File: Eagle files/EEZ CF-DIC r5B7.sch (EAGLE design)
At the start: 277 parts, among them IC1 VIPer35L, IC2 SI8233BB-D-IS1, IC3 LM5041B, IC4 LM258D, IC5 IR11688STRPBF, IC6 LM258D, IC7 TL103W, P1 T910W-50K, Q1 MMBT5551, Q10 BC856C, Q2 C3M0280090D, Q3 C3M0280090D, Q4 NYC0102BLT1G, Q5 IPW60R120P7, Q6 IPW60R120P7, Q7 FDD86250-F085, Q8 FDD86250-F085, Q9 BC856C, X1 39-30-3035, X2 22-05-7095, X3 B2B-ZR, X4 39-30-1020

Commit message: r5B7 BOM
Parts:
- C27, C75: value 47p -> 47p/200V
- C41: value 4n7/500V -> 2n2/1kV
- C57: value UPW1J152MHD -> UVZ1J222MHD
- C63, C70: value 4n7/500V -> 2n2/1kV; device rcl:C-EUC1206 -> rcl:C-EUC1210
- D11, D14: value 1N5819HW-7-F -> N.C.
- Q5, Q6: value IPW60R120P7 -> IRFP4332PBF
- R32: device rcl:R-EU_R1206 -> rcl:R-EU_R0805
- R70, R76: value 1K -> 1K8
- R74: value 100K -> 86K6
- ZD1: value BZX384-C13 -> BZT52C13; device EEZ_Lib1:ZENER-DIODESOD323 -> EEZ_Lib1:ZENER-DIODESOD123
- ZD3: device EEZ_Lib1:ZENER-DIODESOD323 -> EEZ_Lib1:ZENER-DIODESOD123
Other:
- moved on the sheet: R20
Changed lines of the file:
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@@
 <setting verticaltext="up"/>
 </settings>
-<grid distance="0.1" unitdist="inch" unit="inch" style="lines" multiple="1" display="no" altdistance="0.01" altunitdist="inch" altunit="inch"/>
+<grid distance="0.025" unitdist="inch" unit="inch" style="lines" multiple="4" display="no" altdistance="0.01" altunitdist="inch" altunit="inch"/>
 <layers>
 <layer number="1" name="Top" color="4" fill="1" visible="no" active="no"/>
@@
 <part name="R68" library="rcl" deviceset="R-EU_" device="R2512" value="22R/2-3W"/>
 <part name="R77" library="rcl" deviceset="R-EU_" device="R2512" value="22R/2-3W"/>
-<part name="C63" library="rcl" deviceset="C-EU" device="C1206" value="4n7/500V"/>
-<part name="C70" library="rcl" deviceset="C-EU" device="C1206" value="4n7/500V"/>
+<part name="C63" library="rcl" deviceset="C-EU" device="C1210" value="2n2/1kV"/>
+<part name="C70" library="rcl" deviceset="C-EU" device="C1210" value="2n2/1kV"/>
 <part name="R73" library="rcl" deviceset="R-EU_" device="R0805" value="10R"/>
 <part name="C58" library="rcl" deviceset="C-EU" device="C1206" value="1u/100V"/>
 <part name="C66" library="rcl" deviceset="C-EU" device="C1206" value="4u7"/>
-<part name="C57" library="EEZ_Lib1" deviceset="ECAP" device="H35.5A" value="UPW1J152MHD"/>
+<part name="C57" library="EEZ_Lib1" deviceset="ECAP" device="H35.5A" value="UVZ1J222MHD"/>
 <part name="TP1" library="EEZ_Lib1" deviceset="PCB_TEST_TAB" device="SHIELD"/>
 <part name="R18" library="rcl" deviceset="R-EU_" device="R0805" value="1K"/>
@@
 <part name="C10" library="rcl" deviceset="C-EU" device="C0805" value="1u"/>
 <part name="R79" library="rcl" deviceset="R-EU_" device="R0805" value="470R"/>
-<part name="ZD1" library="EEZ_Lib1" deviceset="ZENER-DIODE" device="SOD323" value="BZX384-C13"/>
+<part name="ZD1" library="EEZ_Lib1" deviceset="ZENER-DIODE" device="SOD123" value="BZT52C13"/>
 <part name="R4" library="rcl" deviceset="R-EU_" device="R0805" value="1K8"/>
 <part name="C4" library="rcl" deviceset="C-EU" device="C0603" value="N.C."/>
@@
 <part name="R1" library="rcl" deviceset="R-EU_" device="R0805" value="120R"/>
 <part name="C1" library="rcl" deviceset="C-EU" device="C0805" value="3n3"/>
-<part name="C27" library="rcl" deviceset="C-EU" device="C0805" value="47p"/>
+<part name="C27" library="rcl" deviceset="C-EU" device="C0805" value="47p/200V"/>
 <part name="C21" library="rcl" deviceset="C-EU" device="C0603" value="100n"/>
 <part name="R17" library="rcl" deviceset="R-EU_" device="R0805" value="16K"/>
@@
 <part name="R12" library="rcl" deviceset="R-EU_" device="R0805" value="120R"/>
 <part name="R15" library="rcl" deviceset="R-EU_" device="R0805" value="120R"/>
-<part name="ZD3" library="EEZ_Lib1" deviceset="ZENER-DIODE" device="SOD323" value="MMSZ5V1T1G"/>
+<part name="ZD3" library="EEZ_Lib1" deviceset="ZENER-DIODE" device="SOD123" value="MMSZ5V1T1G"/>
 <part name="SUPPLY77" library="supply2" deviceset="+12V" device=""/>
 <part name="SUPPLY80" library="supply2" deviceset="GND" device=""/>
@@
 <part name="R87" library="rcl" deviceset="R-EU_" device="R0805" value="86K6"/>
 <part name="C78" library="rcl" deviceset="C-EU" device="C0805" value="470p"/>
-<part name="C75" library="rcl" deviceset="C-EU" device="C0805" value="47p"/>
+<part name="C75" library="rcl" deviceset="C-EU" device="C0805" value="47p/200V"/>
 <part name="R92" library="rcl" deviceset="R-EU_" device="R0805" value="7K5"/>
 <part name="R81" library="rcl" deviceset="R-EU_" device="R0805" value="150K"/>
@@
 <part name="JP5" library="EEZ_Lib1" deviceset="JP3-CUT" device=""/>
 <part name="PE4" library="supply1" deviceset="PE" device=""/>
-<part name="R74" library="rcl" deviceset="R-EU_" device="R0805" value="100K"/>
+<part name="R74" library="rcl" deviceset="R-EU_" device="R0805" value="86K6"/>
 <part name="IC5" library="EEZ_Lib1" deviceset="IR11688" device="" value="IR11688STRPBF"/>
 <part name="C5" library="EEZ_Lib1" deviceset="ECAP" device="PANASONIC_H" value="EEEFK1V470P"/>
@@
 <part name="D10" library="EEZ_Lib1" deviceset="SCHOTTKY" device="-SIC_L" value="C3D02065E"/>
 <part name="C31" library="rcl" deviceset="C-EU" device="C0603" value="10n"/>
-<part name="Q6" library="EEZ_Lib1" deviceset="IRFP240" device="" value="IPW60R120P7"/>
-<part name="Q5" library="EEZ_Lib1" deviceset="IRFP240" device="" value="IPW60R120P7"/>
+<part name="Q6" library="EEZ_Lib1" deviceset="IRFP240" device="" value="IRFP4332PBF"/>
+<part name="Q5" library="EEZ_Lib1" deviceset="IRFP240" device="" value="IRFP4332PBF"/>
 <part name="C48" library="rcl" deviceset="C-EU" device="C0603" value="100n"/>
 <part name="R51" library="rcl" deviceset="R-EU_" device="R0805" value="15K"/>
 <part name="C46" library="rcl" deviceset="C-EU" device="C0805" value="1u"/>
-<part name="R32" library="rcl" deviceset="R-EU_" device="R1206" value="86K6"/>
+<part name="R32" library="rcl" deviceset="R-EU_" device="R0805" value="86K6"/>
 <part name="R47" library="rcl" deviceset="R-EU_" device="R0805" value="8K2"/>
 <part name="R45" library="rcl" deviceset="R-EU_" device="R0805" value="1K"/>
@@
 <part name="Q3" library="EEZ_Lib1" deviceset="IRFP240" device="" value="C3M0280090D"/>
 <part name="R26" library="rcl" deviceset="R-EU_" device="R0805" value="10R"/>
-<part name="D11" library="diode" deviceset="DIODE-" device="SOD323-W" value="1N5819HW-7-F"/>
+<part name="D11" library="diode" deviceset="DIODE-" device="SOD323-W" value="N.C."/>
 <part name="R36" library="rcl" deviceset="R-EU_" device="R0805" value="10R"/>
-<part name="D14" library="diode" deviceset="DIODE-" device="SOD323-W" value="1N5819HW-7-F"/>
+<part name="D14" library="diode" deviceset="DIODE-" device="SOD323-W" value="N.C."/>
 <part name="C45" library="rcl" deviceset="C-EU" device="C0603" value="100n"/>
 <part name="D12" library="EEZ_Lib1" deviceset="SCHOTTKY" device="-TO220" value="C3D03060A"/>
@@
 <part name="OK3" library="EEZ_Lib1" deviceset="TLP291" device="" value="TLP291-GB.SE-T"/>
 <part name="SUPPLY60" library="supply2" deviceset="0V" device=""/>
-<part name="C41" library="rcl" deviceset="C-EU" device="C1210" value="4n7/500V"/>
+<part name="C41" library="rcl" deviceset="C-EU" device="C1210" value="2n2/1kV"/>
 <part name="C35" library="EEZ_Lib1" deviceset="ECAP" device="7.5G_18MM" value="UPH2G151MHD6"/>
 <part name="R44" library="rcl" deviceset="R-EU_" device="R0805" value="10R"/>
@@
 <part name="R7" library="rcl" deviceset="R-EU_" device="R0805" value="4K7"/>
 <part name="JP4" library="jump-0r-smd" deviceset="0R-JUMP" device="A"/>
-<part name="R76" library="rcl" deviceset="R-EU_" device="R0805" value="1K"/>
-<part name="R70" library="rcl" deviceset="R-EU_" device="R0805" value="1K"/>
+<part name="R76" library="rcl" deviceset="R-EU_" device="R0805" value="1K8"/>
+<part name="R70" library="rcl" deviceset="R-EU_" device="R0805" value="1K8"/>
 <part name="C71" library="rcl" deviceset="C-EU" device="C0805" value="47p/200V"/>
 <part name="C59" library="rcl" deviceset="C-EU" device="C0805" value="47p/200V"/>
@@
 <attribute name="VALUE" x="203.2" y="68.58" size="1.778" layer="96" rot="R90"/>
 </instance>
-<instance part="R20" gate="G$1" x="66.04" y="27.94" smashed="yes" rot="MR270">
-<attribute name="NAME" x="64.77" y="28.1686" size="1.778" layer="95" rot="MR0"/>
-<attribute name="VALUE" x="64.77" y="25.908" size="1.778" layer="96" rot="MR0"/>
+<instance part="R20" gate="G$1" x="66.04" y="33.02" smashed="yes" rot="MR270">
+<attribute name="NAME" x="64.77" y="33.2486" size="1.778" layer="95" rot="MR0"/>
+<attribute name="VALUE" x="64.77" y="30.988" size="1.778" layer="96" rot="MR0"/>
 </instance>
 <instance part="R14" gate="G$1" x="66.04" y="83.82" smashed="yes" rot="R270">
@@
 <wire x1="53.34" y1="17.78" x2="48.26" y2="17.78" width="0.1524" layer="91"/>
 <pinref part="R20" gate="G$1" pin="2"/>
-<wire x1="66.04" y1="22.86" x2="66.04" y2="17.78" width="0.1524" layer="91"/>
+<wire x1="66.04" y1="27.94" x2="66.04" y2="17.78" width="0.1524" layer="91"/>
 <junction x="66.04" y="17.78"/>
 <pinref part="D9" gate="G$1" pin="A"/>
@@
 <pinref part="IC1" gate="G$1" pin="BR"/>
 <pinref part="R20" gate="G$1" pin="1"/>
-<wire x1="66.04" y1="33.02" x2="66.04" y2="55.88" width="0.1524" layer="91"/>
+<wire x1="66.04" y1="38.1" x2="66.04" y2="55.88" width="0.1524" layer="91"/>
 <pinref part="R14" gate="G$1" pin="2"/>
 <wire x1="66.04" y1="55.88" x2="66.04" y2="78.74" width="0.1524" layer="91"/>
@@
 <instance part="D11" gate="G$1" x="154.94" y="157.48" smashed="yes" rot="R180">
 <attribute name="NAME" x="152.654" y="159.2326" size="1.778" layer="95"/>
-<attribute name="VALUE" x="148.082" y="154.5336" size="1.27" layer="96"/>
+<attribute name="VALUE" x="152.527" y="153.8986" size="1.778" layer="96"/>
 </instance>
 <instance part="R36" gate="G$1" x="147.32" y="127" smashed="yes">
@@
 <instance part="D14" gate="G$1" x="152.4" y="121.92" smashed="yes" rot="R180">
 <attribute name="NAME" x="150.114" y="123.6726" size="1.778" layer="95"/>
-<attribute name="VALUE" x="146.177" y="118.9736" size="1.27" layer="96"/>
+<attribute name="VALUE" x="150.622" y="118.3386" size="1.778" layer="96"/>
 </instance>
 <instance part="C45" gate="G$1" x="109.22" y="88.9" smashed="yes" rot="R90">
@@
 </instance>
 <instance part="C57" gate="G$1" x="149.86" y="157.48" smashed="yes">
-<attribute name="NAME" x="151.003" y="157.9626" size="1.778" layer="95"/>
-<attribute name="VALUE" x="152.2476" y="157.607" size="1.27" layer="96" rot="R270"/>
+<attribute name="NAME" x="150.368" y="157.9626" size="1.778" layer="95"/>
+<attribute name="VALUE" x="150.368" y="152.8826" size="1.27" layer="96"/>
 </instance>
 <instance part="SUPPLY12" gate="GND" x="149.86" y="139.7" smashed="yes">

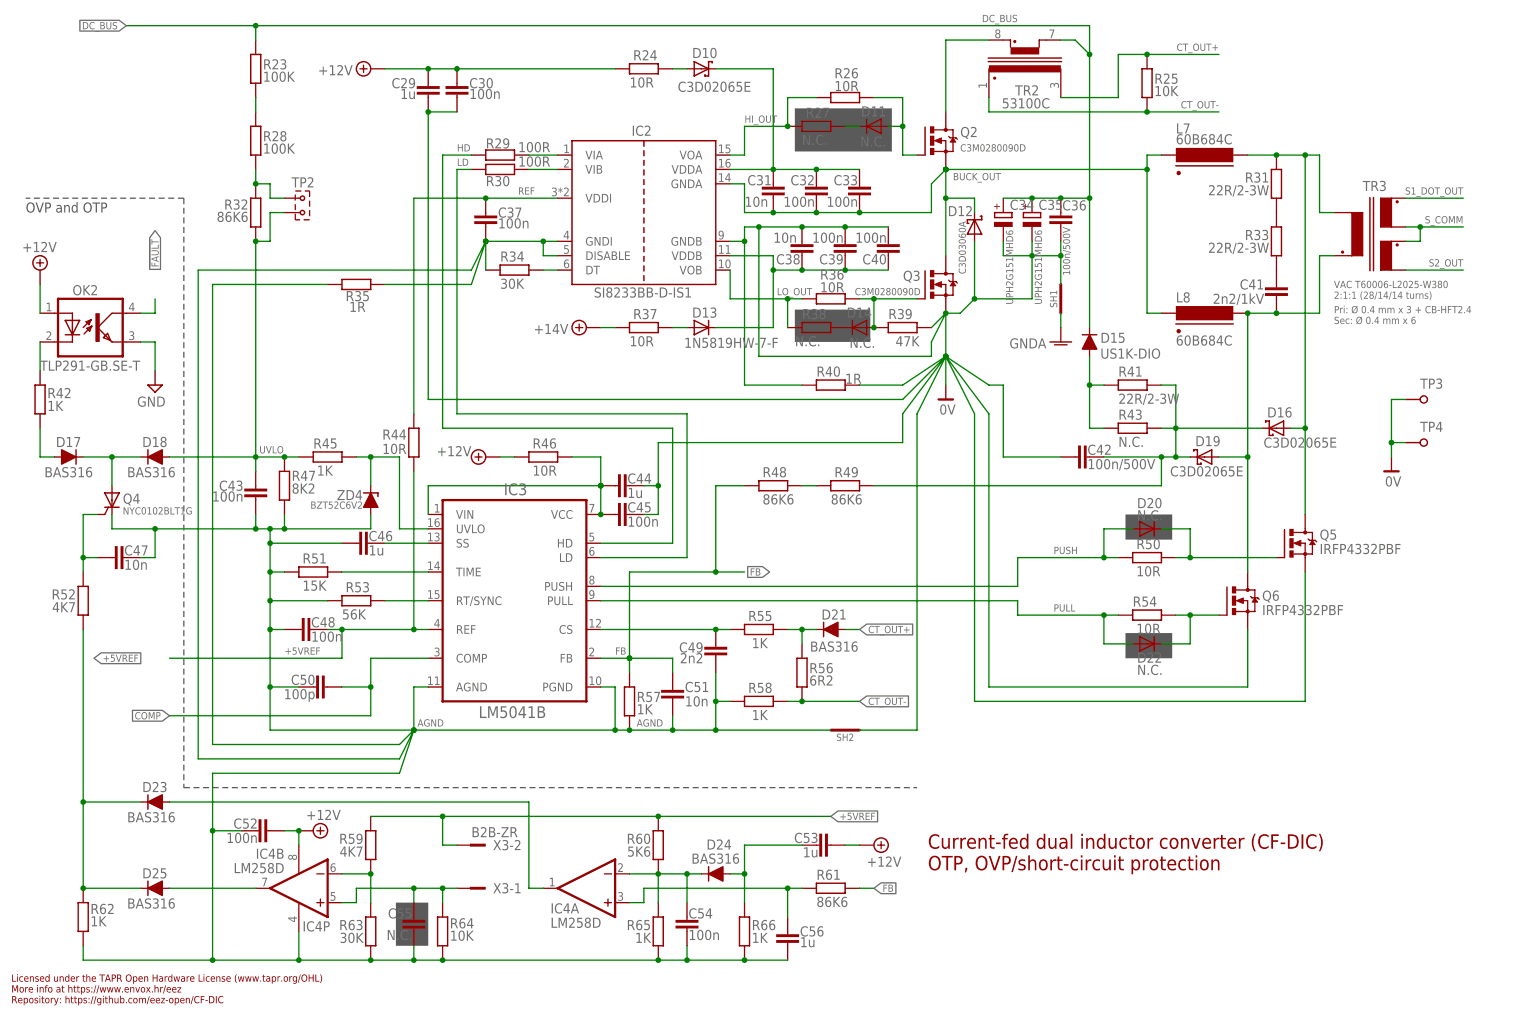
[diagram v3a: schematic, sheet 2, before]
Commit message: NFB compensation and Viper Rovp adjustment
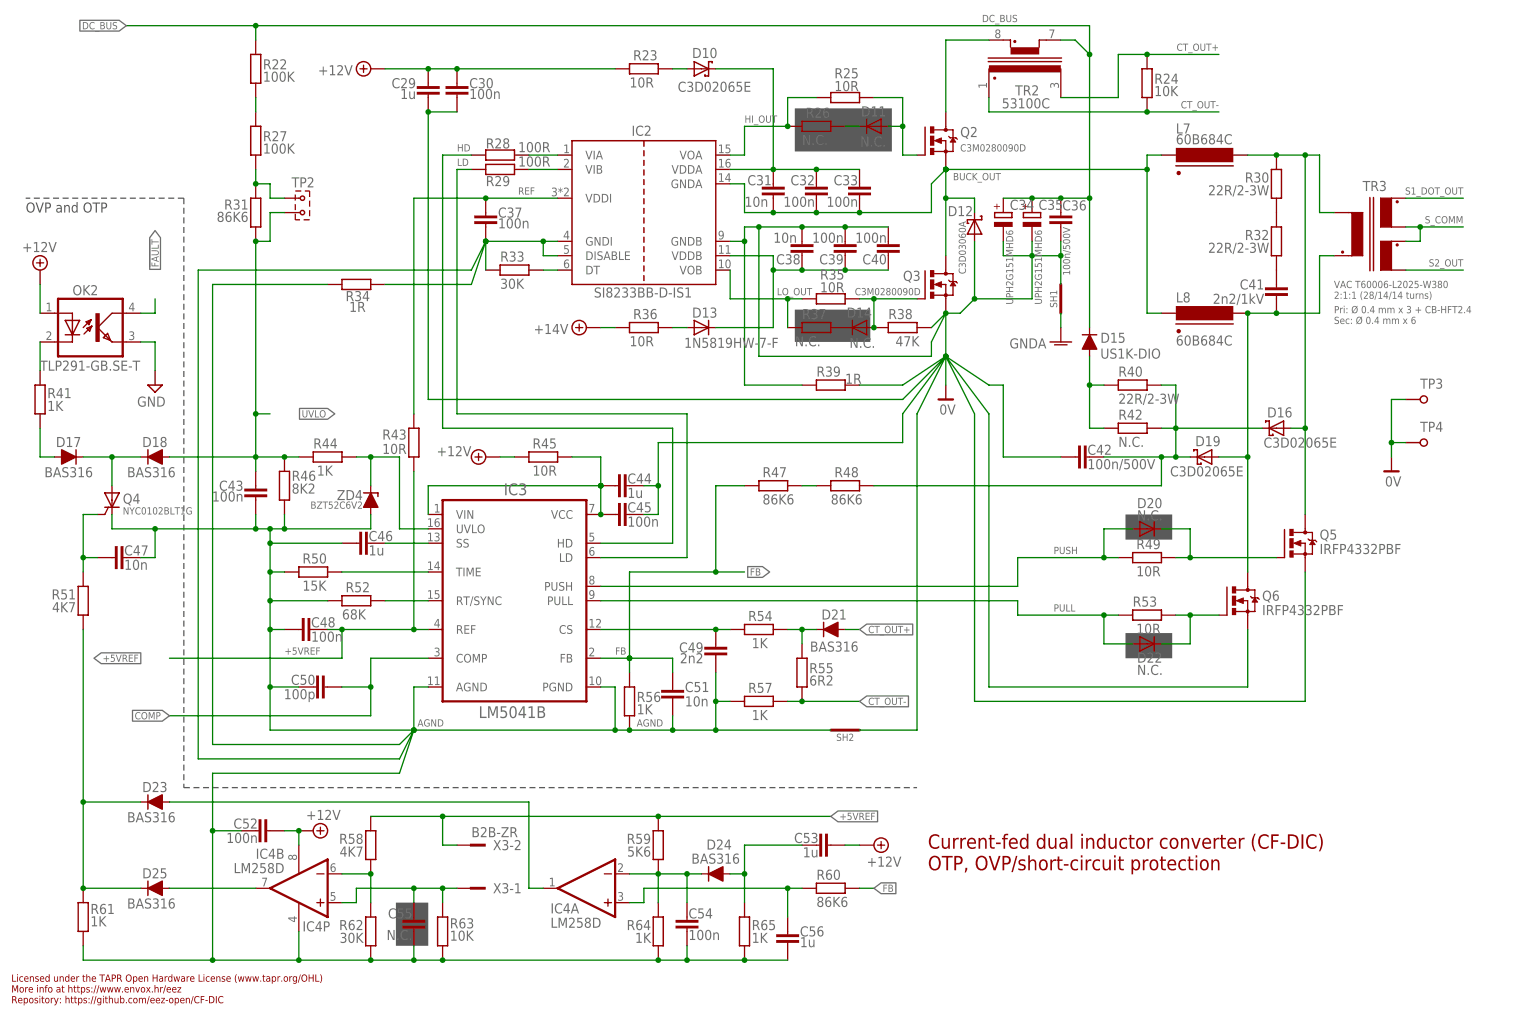
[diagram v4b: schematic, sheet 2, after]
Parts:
- removed R101: 39K, rcl:R-EU_R0805
- C14: value 2n2/1kV -> 1n/1kV
- C73: value 1n -> 2n2
- C78: value 470p -> 1n
- D7: value SS100B -> SS110B
- L9: value IHLP2020CZER3R3M11 -> 3u3/5A; device EEZ_inductors_and_transformers:IHLP-2020BZ-11 -> EEZ_inductors_and_transformers:COILCRAFT_HPI0630
- R100: value 18K -> 39K
- R11, R8: value 36K -> 100K
- R16: value N.C. -> 30K
- R17: value 16K -> 1K
- R18: value 1K -> 1K8
- R20: value 1K8 -> 47K
- R21: value 47K -> 1K
- R22: value 1K -> 100K; device rcl:R-EU_R0805 -> rcl:R-EU_R1206
- R23: value 100K -> 10R; device rcl:R-EU_R1206 -> rcl:R-EU_R0805
- R24: value 10R -> 10K
- R25: value 10K -> 10R
- R26, R37: value 10R -> N.C.
- R27: value N.C. -> 100K; device rcl:R-EU_R0805 -> rcl:R-EU_R1206
- R28: value 100K -> 100R; device rcl:R-EU_R1206 -> rcl:R-EU_R0805
- R30: value 100R -> 22R/2-3W; device rcl:R-EU_R0805 -> rcl:R-EU_R2512
- R31: value 22R/2-3W -> 86K6; device rcl:R-EU_R2512 -> rcl:R-EU_R0805
- R32: value 86K6 -> 22R/2-3W; device rcl:R-EU_R0805 -> rcl:R-EU_R2512
- R33: value 22R/2-3W -> 30K; device rcl:R-EU_R2512 -> rcl:R-EU_R0805
- R34: value 30K -> 1R
- R35: value 1R -> 10R
- R38: value N.C. -> 47K
- R39: value 47K -> 1R
- R40: value 1R -> 22R/2-3W; device rcl:R-EU_R0805 -> rcl:R-EU_R2512
- R41: value 22R/2-3W -> 1K; device rcl:R-EU_R2512 -> rcl:R-EU_R0805
- R42: value 1K -> N.C.; device rcl:R-EU_R0805 -> rcl:R-EU_R2512
- R43, R71: value N.C. -> 10R; device rcl:R-EU_R2512 -> rcl:R-EU_R0805
- R44, R54, R75: value 10R -> 1K
- R45: value 1K -> 10R
- R46: value 10R -> 8K2
- R47: value 8K2 -> 86K6
- R49, R74: value 86K6 -> 10R
- R50: value 10R -> 15K
- R51: value 15K -> 4K7
- R52: value 4K7 -> 68K
- R53: value 56K -> 10R
- R55: value 1K -> 6R2
- R56: value 6R2 -> 1K
- R58, R83: value 1K -> 4K7
- R59: value 4K7 -> 5K6
- R60: value 5K6 -> 86K6
- R61: value 86K6 -> 1K
- R62: value 1K -> 30K
- R63: value 30K -> 10K
- R64, R82: value 10K -> 1K
- R66: value 1K -> 120R
- R67: value 120R -> 22R/2-3W; device rcl:R-EU_R0805 -> rcl:R-EU_R2512
- R68: value 22R/2-3W -> N.C.; device rcl:R-EU_R2512 -> rcl:R-EU_R1210
- R69: value N.C. -> 1K; device rcl:R-EU_R1210 -> rcl:R-EU_R0805
- R70: value 1K8 -> N.C.; device rcl:R-EU_R0805 -> rcl:R-EU_R2512
- R73: value 10R -> 86K6
- R76: value 1K8 -> 22R/2-3W; device rcl:R-EU_R0805 -> rcl:R-EU_R2512
- R77: value 22R/2-3W -> 10K; device rcl:R-EU_R2512 -> rcl:R-EU_R0805
- R78: value 10K -> 470R
- R80: value 470R -> 150K
- R81: value 150K -> 10K
- R84: value 30K -> 1K8
- R85: value 1K8 -> 1K
- R86: value 1K -> 27K
- R87: value 86K6 -> 1K8
- R88: value 1K8 -> 3K3
- R89: value 3K3 -> 1K
- R90: value 1K -> 5K6
- R91: value 5K6 -> 7K5
- R92: value 7K5 -> 220R
- R93: value 220R -> N.C.
- R95: value N.C. -> 10K
- R97: value 10K -> 180K
- R98: value 180K -> 39K
- R99: value 39K -> 18K
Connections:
- net +12V: now also R23.2, R36.2, R45.2; no longer R24.2, R37.2, R46.2
- net +2.5VREF: now also R81.2, R87.1; no longer R82.2, R88.1
- net +5VREF: now also R43.1, R58.2, R95.1, R97.1; no longer R44.1, R60.2, R96.1, R98.1
- net +6V_REC: now also R17.1; no longer R18.1
- net 0V: now also R18.2, R38.2, R39.1; no longer R21.2, R40.1, R40.2
- net AGND: now also R33.1, R34.2, R46.2, R50.2, R52.2, R56.2, R61.2, R96.2, R99.2; no longer R100.2, R35.1, R35.2, R47.2, R51.2, R53.2, R58.2, R66.2, R97.2
- net AUX_AC: no longer R16.2
- net CLAMP_C: now also R40.1, R42.1, R48.2; no longer R41.1, R43.1, R49.2
- net CT_OUT+: now also R24.1; no longer R25.1
- net CT_OUT-: now also R24.2, R55.2, R57.1; no longer R25.2, R56.2, R58.1
- net DC_BUS: now also R22.1; no longer R23.1
- net FB: now also R47.1, R56.1, R60.1; no longer R48.1, R57.1, R61.1
- net FB2: now also R21.1; no longer R22.1
- net G1_OUT: now also R71.1; no longer R72.1
- net G2_OUT: now also R74.1; no longer R75.1
- net GATE1: now also R71.2; no longer R72.2
- net GATE2: now also R74.2; no longer R75.2
- net GND: now also R70.1, R73.2; no longer R71.1, R74.2
- net HD: now also R28.2; no longer R29.2
- net HI_OUT: now also R25.2; no longer R27.2
- net LD: now also R29.2; no longer R30.2
- net LO_OUT: now also R35.1, R37.1; no longer R36.1, R38.1
- net L_PUSH: now also R30.2; no longer R31.2
- net N$10: now also R86.1, R90.1; no longer R87.1, R91.1
- net N$100: now also R51.1; no longer R52.1
- net N$11: now also R79.2; no longer R80.2
- net N$12: now also R80.1, R84.2; no longer R81.1, R85.2
- net N$13: now also R49.1; no longer R50.1
- net N$130: now also R41.2; no longer R42.2
- net N$132: now also R77.2, R81.1; no longer R78.2, R82.1
- net N$134: now also R92.2; no longer R93.2
- net N$135: now also R17.2; no longer R18.2
- net N$14: now also R53.1; no longer R54.1
- net N$141: no longer R17.1
- net N$152: now also R20.1; no longer R21.1
- net N$155: now also R16.2; no longer R17.2
- net N$16: now also R78.2; no longer R79.2
- net N$17: now also R32.1; no longer R33.1
- net N$18: now also R73.1; no longer R74.1
- net N$19: now also R52.1; no longer R53.1
- net N$2: now also R27.2, R31.1; no longer R28.2, R32.1
- net N$20: now also R18.1; no longer R20.1
- net N$21: now also R25.1; no longer R26.1
- net N$22: now also R50.1; no longer R51.1
- net N$25: now also R44.1; no longer R45.1
- net N$26: now also R58.1, R62.1; no longer R59.1, R63.1
- net N$28: now also R83.2; no longer R84.2
- net N$29: now also R35.2, R38.1; no longer R36.2, R39.1
- net N$30: now also R47.2, R48.1; no longer R48.2, R49.1
- net N$31: now also R23.1; no longer R24.1
- net N$32: now also R41.1; no longer R42.1
- net N$34: now also R60.2; no longer R61.2
- net N$35: now also R40.2, R42.2; no longer R41.2, R43.2
- net N$36: now also R28.1; no longer R29.1
- net N$37: now also R54.2; no longer R55.2
- net N$40: now also R29.1; no longer R30.1
- net N$42: now also R63.1; no longer R64.1
- net N$45: now also R26.1; no longer R27.1
- net N$46: now also R72.1, R87.2; no longer R73.1, R89.2
- net N$48: now also R33.2; no longer R34.2
- net N$5: now also R30.1, R32.2; no longer R31.1, R33.2
- net N$50: now also R83.1, R90.2, R93.2; no longer R85.1, R92.2, R94.2
- net N$51: now also R51.2, R61.1; no longer R52.2, R62.1
- net N$52: now also R37.2; no longer R38.2
- net N$53: now also R77.1, R82.2; no longer R78.1, R83.2
- net N$54: now also R45.1; no longer R46.1
- net N$56: now also R54.1; no longer R56.1
- net N$59: now also R65.1; no longer R66.1
- net N$6: now also R22.2, R27.1; no longer R23.2, R28.1
- net N$61: now also R96.1; no longer R97.1
- net N$62: now also R95.2; no longer R96.2
- net N$63: now also R36.1; no longer R37.1
- net N$64: now also R82.1, R85.2, R89.1; no longer R83.1, R86.2, R90.1
- net N$66: now also R76.2; no longer R77.2
- net N$67: now also R67.2; no longer R68.2
- net N$68: now also R98.2, R99.1; no longer R101.1, R99.2
- net N$7: now also R59.1, R64.1; no longer R60.1, R65.1
- net N$70: now also R97.2, R98.1; no longer R98.2, R99.1
- net N$73: now also R93.1, R94.2; no longer R94.1, R95.2
- net N$77: now also R94.1; no longer R95.1
- net N$8: now also R68.1; no longer R69.1
- net N$9: now also R86.2; no longer R87.2
- net NFB_OFFSET: now also R85.1, R91.1; no longer R86.1, R93.1
- net OK_A: now also R88.1; no longer R89.1
- net POUT+: now also R66.1; no longer R67.1
- net PREG_OUT+: now also R66.2, R68.2, R70.2, R80.2; no longer R67.2, R69.2, R71.2, R81.2
- net PULL: now also R53.2; no longer R54.2
- net PUSH: now also R49.2; no longer R50.2
- net REF: now also R43.2; no longer R44.2
- net S1_DOT_OUT: now also R75.1; no longer R77.1
- net S2_OUT: now also R67.1, R69.2; no longer R68.1, R70.2
- net SYNC_VCC: now also R72.2; no longer R73.2
- net UVLO: now also R100.2, R31.2, R44.2, R46.1; no longer R101.2, R32.2, R45.2, R47.1
- net U_MON1: now also R89.2; no longer R90.2
- net V+: now also R21.2, R78.1; no longer R22.2, R80.1
- net VD1: now also R69.1; no longer R70.1
- net VD2: now also R75.2; no longer R76.2
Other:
- note added: "e.g. HPI0630-3R3 or IHLP2020CZER3R3M11"
- note removed: "100R"
- note removed: "10K"
- note removed: "150K"
- note removed: "200K"
- note removed: "2K2"
- note removed: "2K7"
- note removed: "Rff"
- moved on the sheet: R100, R16, R17, R18, R20, R21, R23, R24, R25, R26, R27, R28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
